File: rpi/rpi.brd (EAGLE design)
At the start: 50 x 50 mm, 22 parts, among them IC1 MCP2515-E/SO, IC2 MCP2551, IC3 LM2595NDH

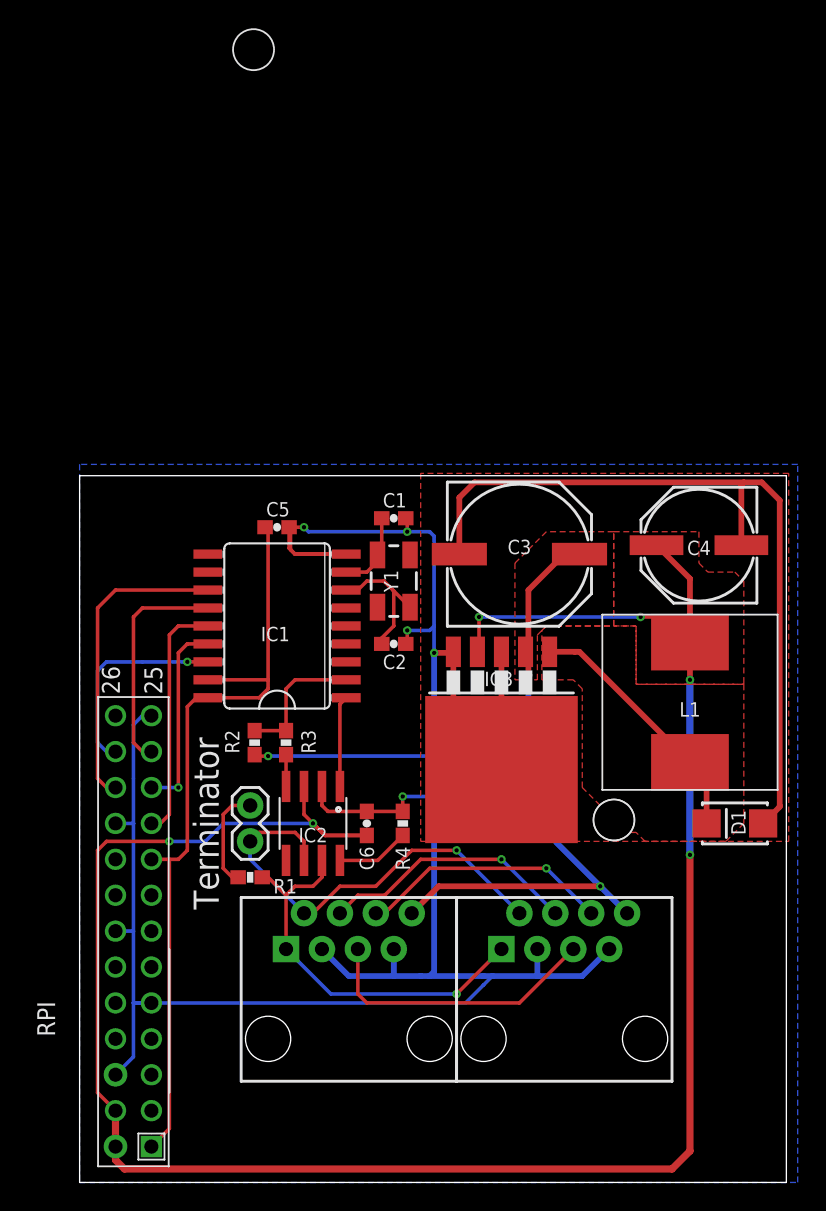
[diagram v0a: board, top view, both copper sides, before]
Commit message: Added power injector board; refactored boards to use MCP2562 instead of MCP2551
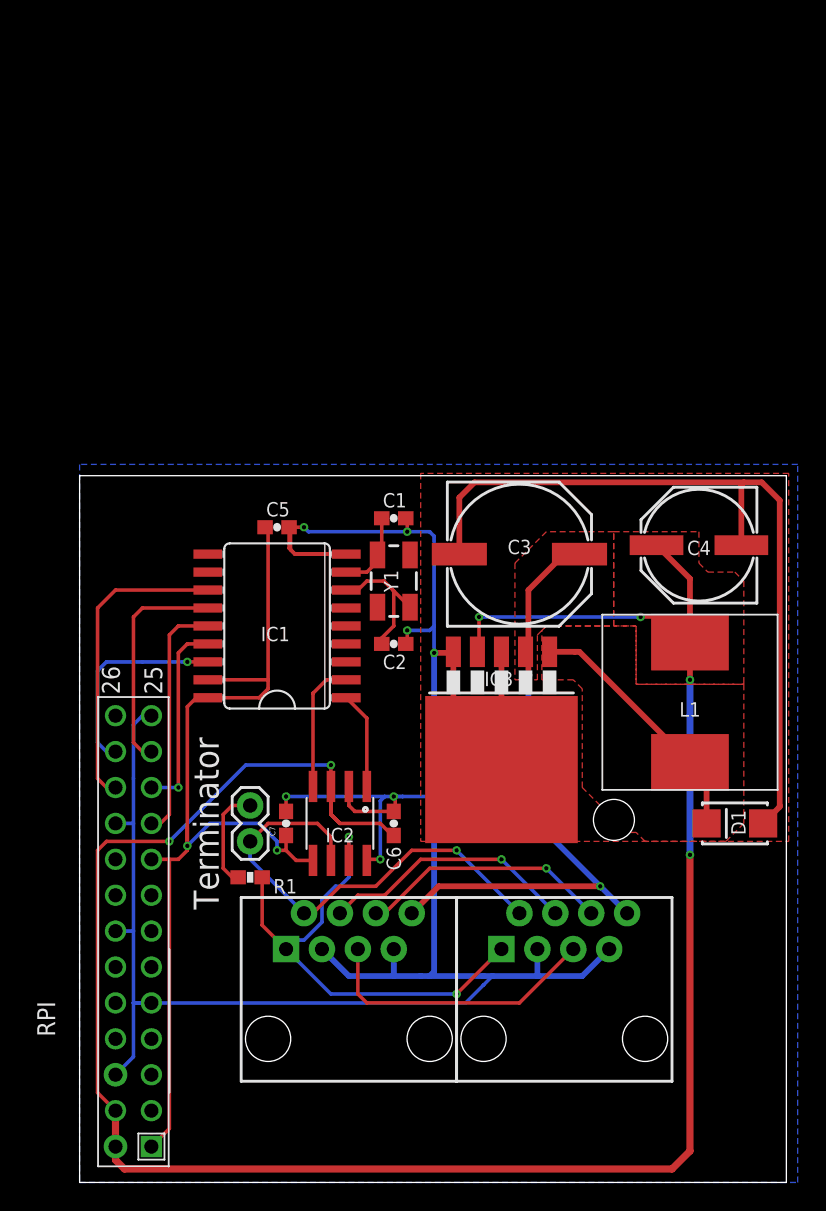
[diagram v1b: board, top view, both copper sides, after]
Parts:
- removed R2: 18k, SparkFun-Passives:0603-RES
- removed R3: 10k, SparkFun-Passives:0603-RES
- removed R4: DNP, SparkFun-Passives:0603-RES
- added C7: 0.1u, SparkFun-Passives:0603-CAP
- IC2: value MCP2551 -> MCP2562; device SparkFun-DigitalIC:SO08 -> nickparts:SO08
- moved C6 1.91 mm to (22.2, 25.4)
- moved IC2 1.90 mm to (18.4, 25.4)
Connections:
- removed net N$1: IC2.4, R3.2
- removed net N$8: IC2.8, R4.2
- net +3V3: now also C7.1, IC2.5
- net GND: now also C7.2, IC2.8; no longer R2.1, R4.1
- net N$2: now also IC2.4; no longer R2.2, R3.1
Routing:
- net +3V3: track 55.8 -> 69.2 mm, vias 0 -> 2
- net CANH: track 28.2 -> 35.7 mm, vias 1 -> 2
- net N$8: track 5.18 -> 0.00 mm
- net +5V: track 155.2 -> 158.4 mm
- net CANL: track 31.3 -> 33.9 mm
- net N$1: track 2.25 -> 0.00 mm
- net GND: track 237.9 -> 238.5 mm, vias 6 -> 7
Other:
- board text added: "uCAN RPi v1.0"

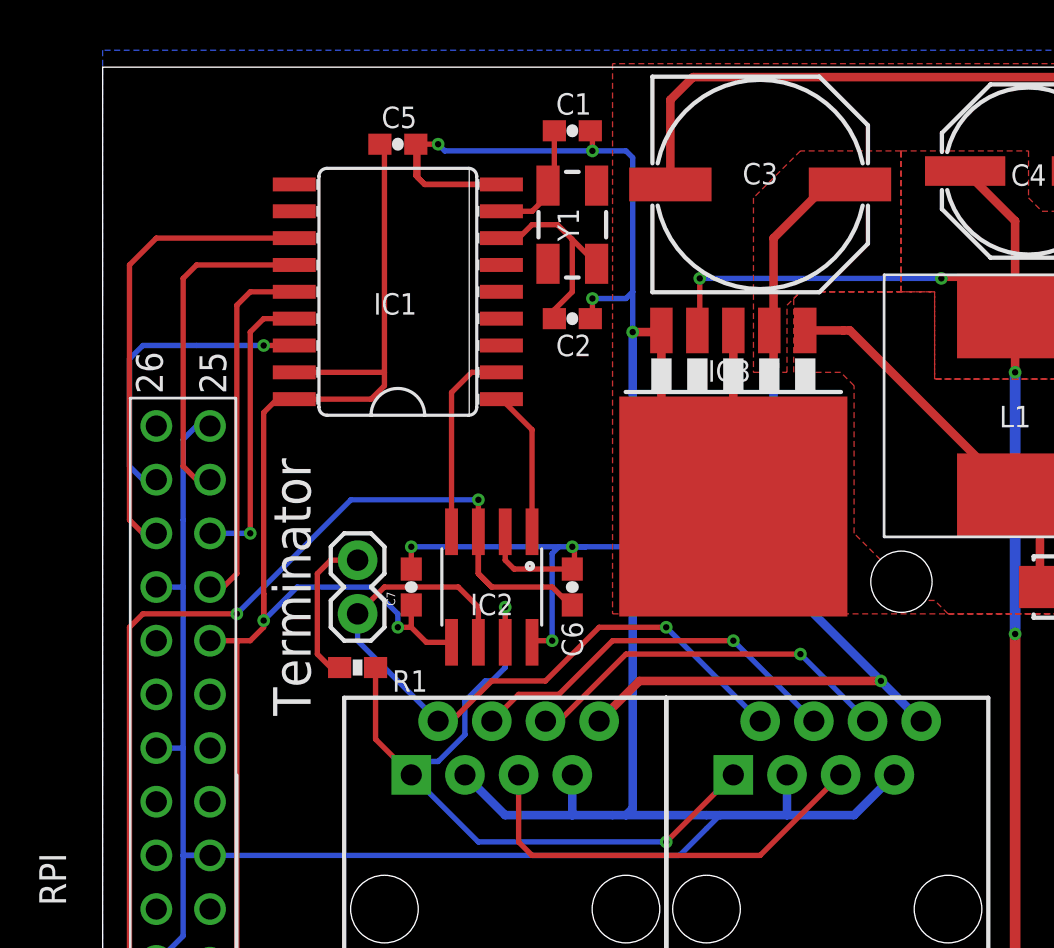
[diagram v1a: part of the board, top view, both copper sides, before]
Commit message: Switch to split termination with a switch
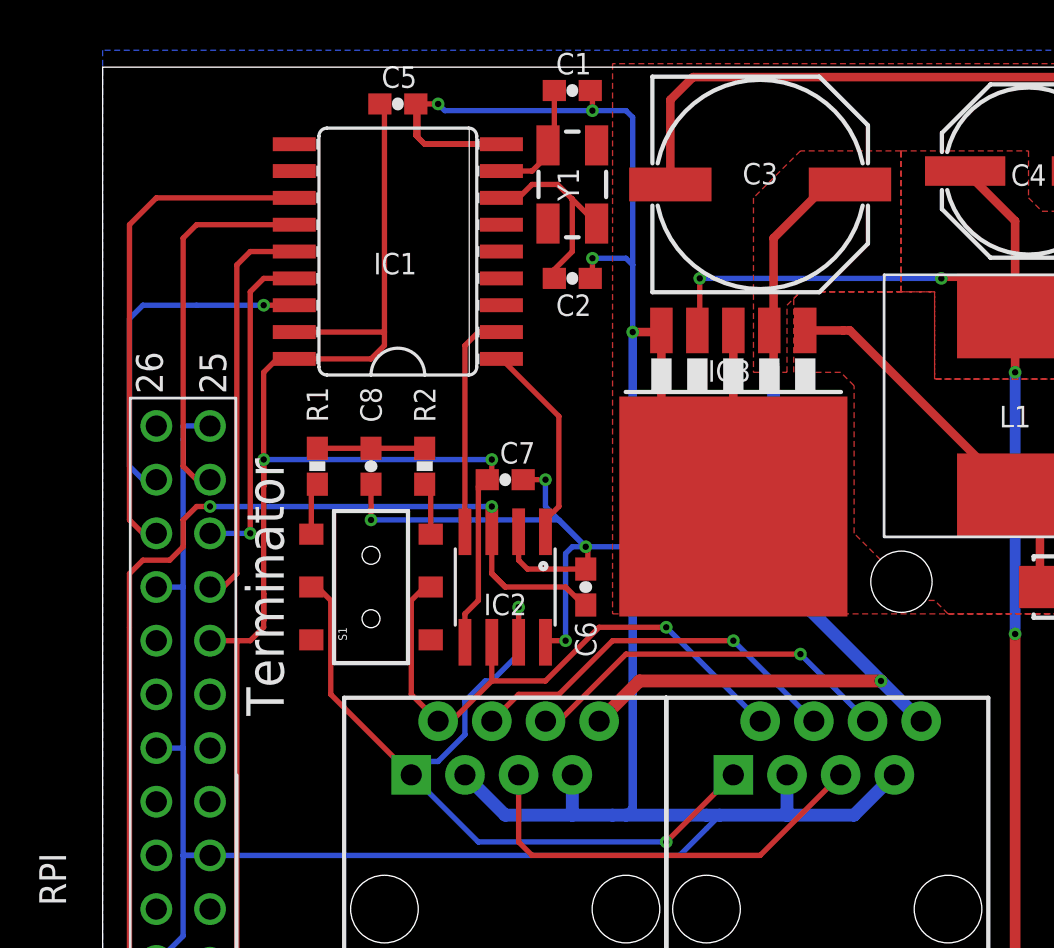
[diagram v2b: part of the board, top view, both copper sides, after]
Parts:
- removed JP1: (no value), SparkFun-Passives:1X02
- added C8: 4.7n, SparkFun-Passives:0603-CAP
- added R2: 60, SparkFun-Passives:0603-RES
- added S1: DPDT, SparkFun-Electromechanical:AYZ0202
- R1: value 120 -> 60
- moved R1 9.71 mm to (10.2, 31.1), turned to 270 degrees
- moved C7 6.75 mm to (19.1, 30.5), turned to 0 degrees
- moved C1 1.91 mm to (22.2, 48.9)
- moved C2 1.91 mm to (22.2, 40.0)
- moved C5 1.91 mm to (14.0, 48.3)
- moved IC1 1.91 mm to (14.0, 41.3)
- moved Y1 1.91 mm to (22.2, 44.5)
- moved IC2 0.64 mm to (19.1, 25.4)
- moved C6 0.63 mm to (22.9, 25.4)
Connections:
- new net N$1: R1.2, S1.3
- new net N$8: C8.1, R1.1, R2.1
- net CANH: now also S1.2; no longer R1.2
- net CANL: now also S1.5; no longer JP1.1
- net GND: now also C8.2
- net N$7: now also R2.2, S1.6; no longer JP1.2, R1.1
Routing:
- net +3V3: track 69.2 -> 80.4 mm
- net GND: track 238.5 -> 248.9 mm, vias 7 -> 8
- net CANL: track 33.9 -> 28.2 mm
- net CANH: track 35.7 -> 41.1 mm
- net N$8: track 0.00 -> 5.08 mm
- net N$7: track 7.30 -> 2.48 mm
- net N$3: track 6.87 -> 9.57 mm
- net N$1: track 0.00 -> 2.48 mm
- net SPI0_MOSI: track 17.2 -> 19.1 mm
- net SPI0_CE0: track 14.7 -> 16.6 mm
- net CAN_INT: track 21.9 -> 23.8 mm
- net SPI0_SCLK: track 15.9 -> 17.8 mm
- net SPI0_MISO: track 13.8 -> 15.7 mm
- net N$2: track 9.35 -> 10.8 mm

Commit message: Added TVS diodes, fixed silkscreen issues
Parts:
- added IC4: PESD1CAN, nickparts:SOT23
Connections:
- net CANH: now also IC4.1
- net CANL: now also IC4.2
- net GND: now also IC4.3
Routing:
- net CANL: track 28.2 -> 35.1 mm, vias 1 -> 2
- net CANH: track 41.1 -> 46.6 mm
- net GND: track 248.9 -> 252.8 mm, vias 8 -> 9
- net +5V: track 158.8 -> 160.2 mm
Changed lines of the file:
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@@
 </element>
 <element name="IC3" library="nickparts" package="TO263-5" value="LM2595NDH" x="29.845" y="31.75" smashed="yes" rot="R180">
-<attribute name="NAME" x="29.6545" y="35.1155" size="1.016" layer="25" font="vector" ratio="15" align="bottom-center"/>
+<attribute name="NAME" x="35.3695" y="36.3855" size="1.016" layer="25" font="vector" ratio="15" align="bottom-center"/>
 </element>
 <element name="C3" library="SparkFun-Capacitors" package="PANASONIC_G" value="" x="31.115" y="44.45" smashed="yes">
@@
 <attribute name="NAME" x="18.796" y="31.242" size="1.016" layer="25" font="vector" ratio="15"/>
 </element>
-<element name="S1" library="SparkFun-Electromechanical" package="AYZ0202" value="DPDT" x="12.7" y="25.4" rot="R90">
+<element name="S1" library="SparkFun-Electromechanical" package="AYZ0202" value="DPDT" x="12.7" y="25.4" smashed="yes" rot="R90">
 <attribute name="PROD_ID" value="SWCH-08179" x="12.7" y="25.4" size="1.778" layer="27" rot="R90" display="off"/>
+<attribute name="NAME" x="12.7" y="22.098" size="1.016" layer="25" font="vector" ratio="15" align="bottom-center"/>
 </element>
 <element name="R2" library="SparkFun-Passives" package="0603-RES" value="60" x="15.24" y="31.115" smashed="yes" rot="R270">
@@
 <element name="C8" library="SparkFun-Passives" package="0603-CAP" value="4.7n" x="12.7" y="31.115" smashed="yes" rot="R270">
 <attribute name="NAME" x="12.192" y="34.8615" size="1.016" layer="25" font="vector" ratio="15" rot="R270"/>
+</element>
+<element name="IC4" library="nickparts" package="SOT23" value="PESD1CAN" x="8.89" y="15.5575" smashed="yes" rot="R90">
+<attribute name="NAME" x="8.8265" y="13.843" size="1.016" layer="25" font="vector" ratio="15" rot="R180" align="bottom-center"/>
 </element>
 </elements>
@@
 <wire x1="21.9075" y1="25.4" x2="19.05" y2="25.4" width="0.254" layer="1"/>
 <wire x1="19.05" y1="25.4" x2="18.415" y2="26.035" width="0.254" layer="1"/>
-<wire x1="18.415" y1="28.0162" x2="18.415" y2="29.21" width="0.254" layer="1"/>
-<via x="18.415" y="29.21" extent="1-16" drill="0.3"/>
-<wire x1="18.415" y1="29.21" x2="18.0975" y2="29.21" width="0.254" layer="16"/>
+<via x="19.05" y="29.5275" extent="1-16" drill="0.3"/>
 <wire x1="18.0975" y1="29.21" x2="5.08" y2="29.21" width="0.254" layer="16"/>
 <via x="5.08" y="29.21" extent="1-16" drill="0.3"/>
@@
 <wire x1="1.905" y1="26.67" x2="1.27" y2="26.035" width="0.254" layer="1"/>
 <wire x1="1.27" y1="26.035" x2="1.27" y2="23.495" width="0.254" layer="1"/>
+<wire x1="18.415" y1="28.0162" x2="18.415" y2="28.8925" width="0.254" layer="1"/>
+<wire x1="18.415" y1="28.8925" x2="19.05" y2="29.5275" width="0.254" layer="1"/>
+<wire x1="18.0975" y1="29.21" x2="18.7325" y2="29.21" width="0.254" layer="16"/>
+<wire x1="18.7325" y1="29.21" x2="19.05" y2="29.5275" width="0.254" layer="16"/>
 </signal>
 <signal name="GND">
@@
 </polygon>
 <wire x1="24.765" y1="30.1625" x2="25.0825" y2="29.845" width="0.254" layer="16"/>
-<wire x1="5.08" y1="12.7" x2="27.305" y2="12.7" width="0.254" layer="16"/>
+<wire x1="5.08" y1="12.7" x2="8.89" y2="12.7" width="0.254" layer="16"/>
+<wire x1="8.89" y1="12.7" x2="27.305" y2="12.7" width="0.254" layer="16"/>
 <wire x1="27.305" y1="12.7" x2="28.575" y2="13.97" width="0.254" layer="16"/>
 <wire x1="28.575" y1="13.97" x2="29.21" y2="14.605" width="0.254" layer="16"/>
@@
 <wire x1="12.7" y1="28.575" x2="21.59" y2="28.575" width="0.254" layer="16"/>
 <wire x1="21.59" y1="28.575" x2="22.86" y2="27.305" width="0.254" layer="16"/>
+<contactref element="IC4" pad="3"/>
+<wire x1="7.79" y1="15.5575" x2="8.89" y2="15.5575" width="0.254" layer="1"/>
+<via x="8.89" y="15.5575" extent="1-16" drill="0.3"/>
+<wire x1="8.89" y1="15.5575" x2="8.89" y2="12.7" width="0.254" layer="16"/>
+<wire x1="25.0825" y1="47.625" x2="26.865" y2="48.455" width="0" layer="19" extent="1-16"/>
 </signal>
 <signal name="SPI0_CE0">
@@
 <wire x1="10.795" y1="24.765" x2="10.795" y2="20.32" width="0.254" layer="1"/>
 <wire x1="10.795" y1="20.32" x2="14.605" y2="16.51" width="0.254" layer="1"/>
+<contactref element="IC4" pad="1"/>
+<wire x1="9.99" y1="14.6075" x2="12.7025" y2="14.6075" width="0.254" layer="1"/>
+<wire x1="12.7025" y1="14.6075" x2="14.605" y2="16.51" width="0.254" layer="1"/>
 </signal>
 <signal name="CANL">
@@
 <wire x1="14.605" y1="20.32" x2="15.875" y2="19.05" width="0.254" layer="1"/>
 <wire x1="18.415" y1="22.7838" x2="18.415" y2="20.955" width="0.254" layer="1"/>
+<contactref element="IC4" pad="2"/>
+<wire x1="9.99" y1="16.5075" x2="11.4275" y2="16.5075" width="0.254" layer="1"/>
+<wire x1="11.4275" y1="16.5075" x2="11.43" y2="16.51" width="0.254" layer="1"/>
+<via x="11.43" y="16.51" extent="1-16" drill="0.3"/>
+<wire x1="11.43" y1="16.51" x2="13.97" y2="19.05" width="0.254" layer="16"/>
+<wire x1="13.97" y1="19.05" x2="15.875" y2="19.05" width="0.254" layer="16"/>
 </signal>
 <signal name="N$10">
@@
 </signal>
 </signals>
-<errors>
-</errors>
 </board>
 </drawing>

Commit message: Minor changes to shield, rpi board, and cape
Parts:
- removed L1: MSS1260, nickparts:MSS1260
- added C10: 56u, nickparts:SM_RADIAL_6.3AMM
- added C9: 10n, nickparts:0805
- added I1: SRN8040-330M, nickparts:SRN8040
- C3: value (none) -> 4.7u; device SparkFun-Capacitors:PANASONIC_G -> nickparts:1206
- C4: value (none) -> 1u; device SparkFun-Capacitors:PANASONIC_E -> nickparts:0805
- D1: value (none) -> B240A-13-F; device SparkFun-DiscreteSemi:SMA-DIODE_ALT -> nickparts:SMA
- IC3: value LM2595NDH -> LM22675MR-5.0/NOPB; device nickparts:TO263-5 -> nickparts:MRA08B
- moved C4 22.7 mm to (28.9, 27.9)
- moved C3 22.3 mm to (29.8, 22.2), turned to 180 degrees
- moved D1 16.5 mm to (29.8, 25.1)
- moved U$2 4.76 mm to (34.3, 5.40)
- moved U$3 4.76 mm to (19.1, 5.40)
- moved IC3 1.42 mm to (29.2, 33.0), turned to 270 degrees
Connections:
- removed net N$10 (its old number): U$2.4, U$3.4
- removed net N$6: D1.C, IC3.1, L1.P$1
- new net N$9: U$2.3, U$3.3
- new net SWOUT: C9.2, D1.1, I1.2, IC3.8
- net +5V: now also C10.1, I1.1; no longer C4.+, L1.P$2
- net GND: now also C10.2, C3.2, C4.2, D1.2, IC3.EPAD, U$2.8, U$3.8; no longer C3.-, C4.-, D1.A, IC3.3, IC3.5, U$2.3, U$3.3
- net N$11: now also C9.1, IC3.1; no longer U$2.5, U$3.5
- net VCC: now also C3.1, C4.1, IC3.7, U$2.4, U$2.5, U$3.4, U$3.5; no longer C3.+, IC3.2, U$2.8, U$3.8
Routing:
- net GND: track 252.8 -> 178.7 mm, vias 9 -> 18
- net N$6: track 19.2 -> 0.00 mm
- net N$10 (its old number): track 18.4 -> 0.00 mm, vias 1 -> 0
- net N$9: track 0.00 -> 18.4 mm, vias 0 -> 1
- net SWOUT: track 0.00 -> 18.1 mm
- net N$11: track 20.3 -> 2.62 mm
- net CANL: track 35.1 -> 47.4 mm, vias 2 -> 1
- net VCC: track 45.3 -> 38.7 mm, vias 2 -> 0
- net CANH: track 46.6 -> 51.9 mm, vias 2 -> 3
- net +5V: track 160.2 -> 165.2 mm, vias 6 -> 5
- net N$10: track 17.9 -> 22.8 mm, vias 1 -> 0
- added copper zone on layer 1, net SWOUT
- removed copper zone on layer 1, net N$6
- removed copper zone on layer 1, net VCC
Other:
- board text added: "uCAN RPi v1.0.1"
- board text removed: "uCAN RPi v1.0"
